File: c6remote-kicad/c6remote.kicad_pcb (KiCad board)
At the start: 2 copper layers, 37 x 130 mm, 47 parts, among them J1 Battery, Q1 MMBT2222A, SW1 SW_Push, SW10 SW_Push, SW11 SW_Push, SW2 SW_Push, SW3 SW_Push, SW4 SW_Push, SW5 SW_Push, SW6 SW_Push, SW7 SW_Push, SW8 SW_Push, SW9 SW_Push, U1 XIAO-ESP32-C6, U2 TSOP4136, U3 PCF8575DBR

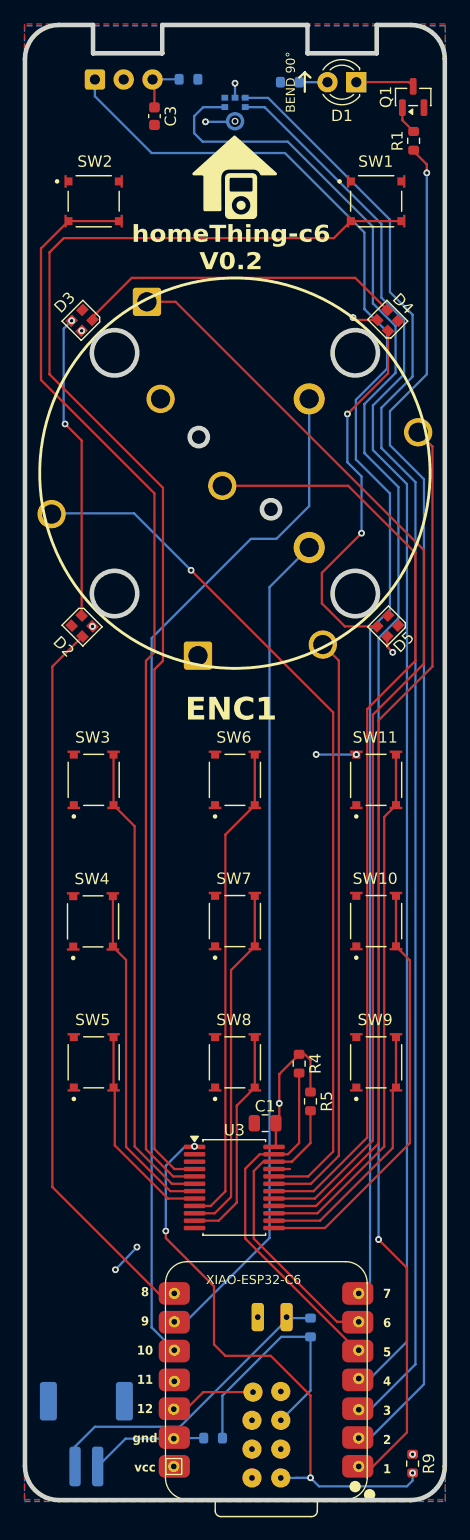
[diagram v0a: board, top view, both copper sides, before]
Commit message: feat(pcb): simplify the top board edge by dropping the two IR cutouts, removing 8 Edge.Cuts segments so the 6.1x2.5mm notches at x 40.837..46.937 and x 59.737..65.837 give way to one straight 31mm line from (37.837455, 28.214) to (68.837455, 28.214) between the corner arcs, neither notch was doing work since U2 topped out at y 31.5 and the D1 dome at y 31.758, both well clear of the old notch floor at y 30.714; the freed strip lets the top row move up, U2 41.0,33.02 to 40.982545,31.262, D1 64.037455,33.258 to 64.0,31.25, R3 and R6 to y 31.25, MK1 53.35,35.99 to 53.35,32.292 and C3 46.25,36.25 to 46.25,34.525, with tracks stretched to follow so segments stay at 289 and vias at 23 while total track length goes 2075.156mm to 2082.025mm, footprints unchanged at 47; zones refilled in the GUI and verified current, a pcbnew ZONE_FILLER pass on a copy reproduces the stored fills exactly with area delta 0 on both the F.Cu GND and +3.3V pours; validated ERC 0, DRC 43 violations 0 errors 0 unconnected parity 13, down from 46 because silk_edge_clearance drops 7 to 4 as three of the four U2 back-silk clips were against the notch walls, all other types unchanged at 24 silk_over_copper, 14 lib_footprint_mismatch and 1 silk_overlap, identical with and without --refill-zones; fab outputs regenerated and export.zip rebuilt from the 11 gerber, job and drill files
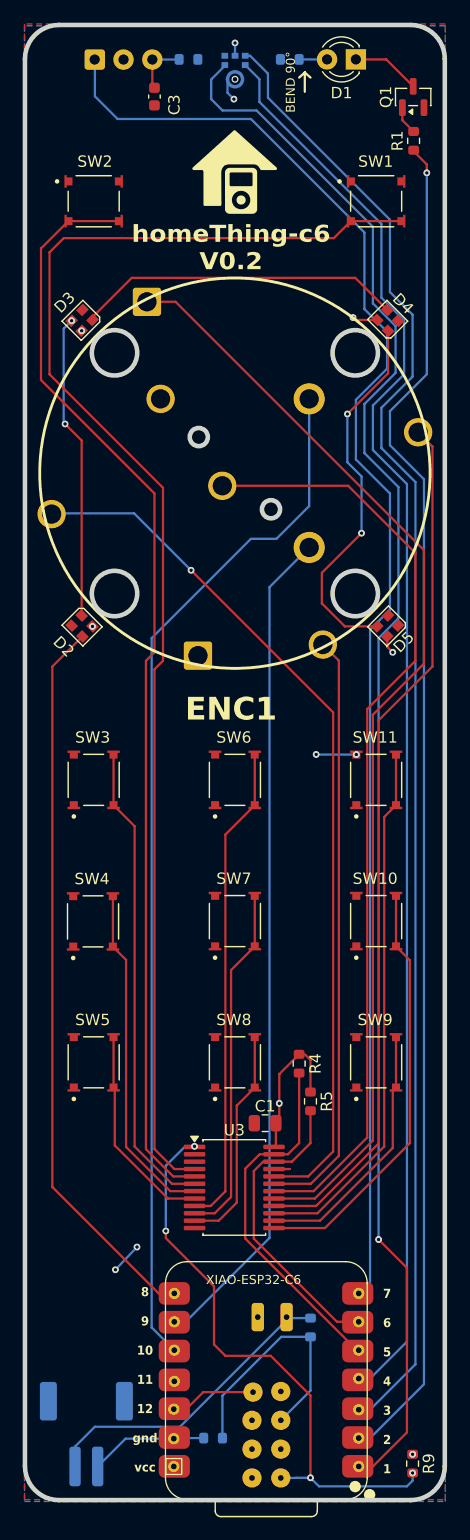
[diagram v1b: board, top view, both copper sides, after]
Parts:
- moved MK1 3.70 mm to (53.4, 32.3)
- moved D1 2.01 mm to (64.0, 31.2)
- moved R3 2.01 mm to (58.2, 31.2)
- moved U2 1.76 mm to (41.0, 31.3)
- moved R6 1.75 mm to (49.2, 31.2)
- moved C3 1.73 mm to (46.2, 34.5)
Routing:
- net sck: track 128.1 -> 130.8 mm
- net ws: track 123.6 -> 126.3 mm
- net IR REC: track 128.1 -> 129.8 mm
- net sd: track 140.4 -> 139.1 mm
- net Net-(D1-K): track 5.17 -> 6.03 mm
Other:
- outline, holes or cut-outs redrawn

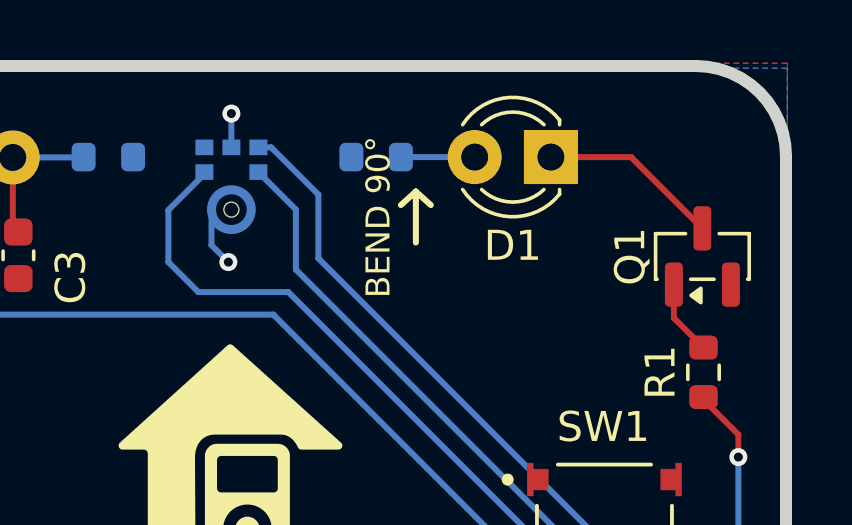
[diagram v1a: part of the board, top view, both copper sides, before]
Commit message: feat(silk): mark the mic port on the front, adding a 2.3mm ring concentric with the MK1 acoustic NPTH at (53.35, 33.002) plus a 1.8mm microphone glyph above it, all five items board graphics on F.SilkS rather than footprint fields so nothing lands in the position file or BOM, ring is a 0.15-wide gr_circle at r 1.15 held under the 1.75mm reach of the neighbouring F.Cu via so its outer edge clears that pad, glyph is a 0.8-wide round-cap gr_line capsule from (53.35, 30.0) to (53.35, 30.3) inside a downward gr_arc bracket (54.2, 30.2) mid (53.35, 31.05) to (52.5, 30.2) with a stem to y 31.05..31.3 and a 1.2mm base at y 31.3, sitting 1.39mm clear of the top board edge; D1 nudged down to y 32.275, R3 across to x 58.425 and the BEND 90 arrow right to x 60.0..61.0 to open the space, tracks following so nets stay intact; zones verified current, a pcbnew ZONE_FILLER pass on a copy reproduces the stored fills exactly with area delta 0 on the GND and +3.3V pours; validated ERC 0, DRC 43 violations 0 errors 0 unconnected parity 13 with the type breakdown unchanged at 24 silk_over_copper, 14 lib_footprint_mismatch, 4 silk_edge_clearance and 1 silk_overlap, so the new silk adds no warnings; fab outputs regenerated and export.zip rebuilt from the 11 gerber, job and drill files
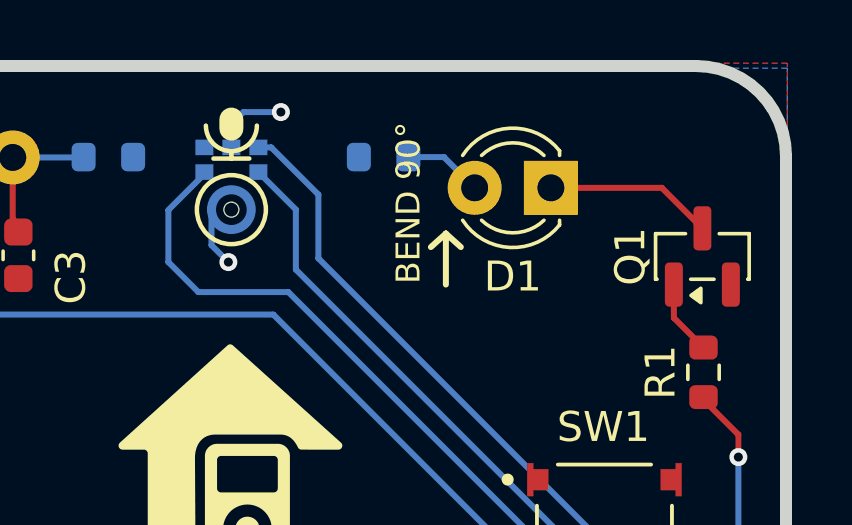
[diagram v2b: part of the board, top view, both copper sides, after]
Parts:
- moved D1 1.02 mm to (64.0, 32.3)
- moved R3 0.25 mm to (58.4, 31.2)
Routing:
- net GND: track 21.2 -> 22.6 mm
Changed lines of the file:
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@@
 	(footprint "LED_THT:LED_D3.0mm_IRBlack"
 		(layer "F.Cu")
-		(at 64 31.25 180)
+		(at 64 32.275 180)
 		(descr "LED, diameter 3.0mm, 2 pins, infrared, black, generated by kicad-footprint-generator")
 		(tags "LED IR")
@@
 		)
 		(point
-			(at 62.73 31.25)
+			(at 62.73 32.275)
 			(size 2)
 			(layer "F.Fab")
@@
 	(footprint "Resistor_SMD:R_0603_1608Metric"
 		(layer "B.Cu")
-		(at 58.175 31.25)
+		(at 58.425 31.25)
 		(descr "Resistor SMD 0603 (1608 Metric), square (rectangular) end terminal, IPC-7351 nominal, (Body size source: IPC-SM-782 page 72, https://www.pcb-3d.com/wordpress/wp-content/uploads/ipc-sm-782a_amendment_1_and_2.pdf)")
 		(tags "resistor")
@@
 	)
 	(gr_line
-		(start 59.5 32.4)
-		(end 59 32.85)
+		(start 52.75 31.3)
+		(end 53.95 31.3)
+		(stroke
+			(width 0.15)
+			(type default)
+		)
+		(layer "F.SilkS")
+	)
+	(gr_line
+		(start 53.35 30)
+		(end 53.35 30.3)
+		(stroke
+			(width 0.8)
+			(type default)
+		)
+		(layer "F.SilkS")
+	)
+	(gr_line
+		(start 53.35 31.05)
+		(end 53.35 31.3)
+		(stroke
+			(width 0.15)
+			(type default)
+		)
+		(layer "F.SilkS")
+	)
+	(gr_circle
+		(center 53.35 33.002)
+		(end 54.5 33.002)
+		(stroke
+			(width 0.15)
+			(type default)
+		)
+		(fill no)
+		(layer "F.SilkS")
+	)
+	(gr_arc
+		(start 54.2 30.2)
+		(mid 53.35 31.05)
+		(end 52.5 30.2)
+		(stroke
+			(width 0.15)
+			(type default)
+		)
+		(layer "F.SilkS")
+	)
+	(gr_line
+		(start 60.5 33.8)
+		(end 60 34.25)
 		(stroke
 			(width 0.2)
@@
 	)
 	(gr_line
-		(start 59.5 32.4)
-		(end 60 32.85)
+		(start 60.5 33.8)
+		(end 61 34.25)
 		(stroke
 			(width 0.2)
@@
 	)
 	(gr_line
-		(start 59.5 34.1)
-		(end 59.5 32.4)
+		(start 60.5 35.5)
+		(end 60.5 33.8)
 		(stroke
 			(width 0.2)
@@
 	)
 	(gr_text "BEND 90°"
-		(at 58.25 33.25 90)
+		(at 59.25 32.775 90)
 		(layer "F.SilkS")
 		(effects
@@
 	)
 	(via
-		(at 53.35 29.8)
+		(at 55 29.75)
 		(size 0.6)
 		(drill 0.3)
@@
 	)
 	(segment
+		(start 53.75 29.75)
+		(end 53.35 30.15)
+		(width 0.2)
+		(layer "B.Cu")
+		(net "GND")
+	)
+	(segment
+		(start 53.35 30.15)
+		(end 53.35 30.928)
+		(width 0.2)
+		(layer "B.Cu")
+		(net "GND")
+	)
+	(segment
 		(start 44.709 135.914)
 		(end 42.809 137.914)
@@
 	)
 	(segment
-		(start 53.35 29.8)
-		(end 53.35 30.928)
+		(start 55 29.75)
+		(end 53.75 29.75)
 		(width 0.2)
 		(layer "B.Cu")
@@
 	)
 	(segment
-		(start 69.05 33.625)
-		(end 66.675 31.25)
+		(start 67.7 32.275)
+		(end 64 32.275)
 		(width 0.2)
 		(layer "F.Cu")
@@
 	)
 	(segment
-		(start 66.675 31.25)
-		(end 64 31.25)
+		(start 69.05 33.625)
+		(end 67.7 32.275)
 		(width 0.2)
 		(layer "F.Cu")
@@
 	)
 	(segment
-		(start 59 31.25)
-		(end 61.46 31.25)
+		(start 60.435 31.25)
+		(end 59.25 31.25)
+		(width 0.2)
+		(layer "B.Cu")
+		(net "Net-(D1-A)")
+	)
+	(segment
+		(start 60.435 31.25)
+		(end 61.46 32.275)
 		(width 0.2)
 		(layer "B.Cu")

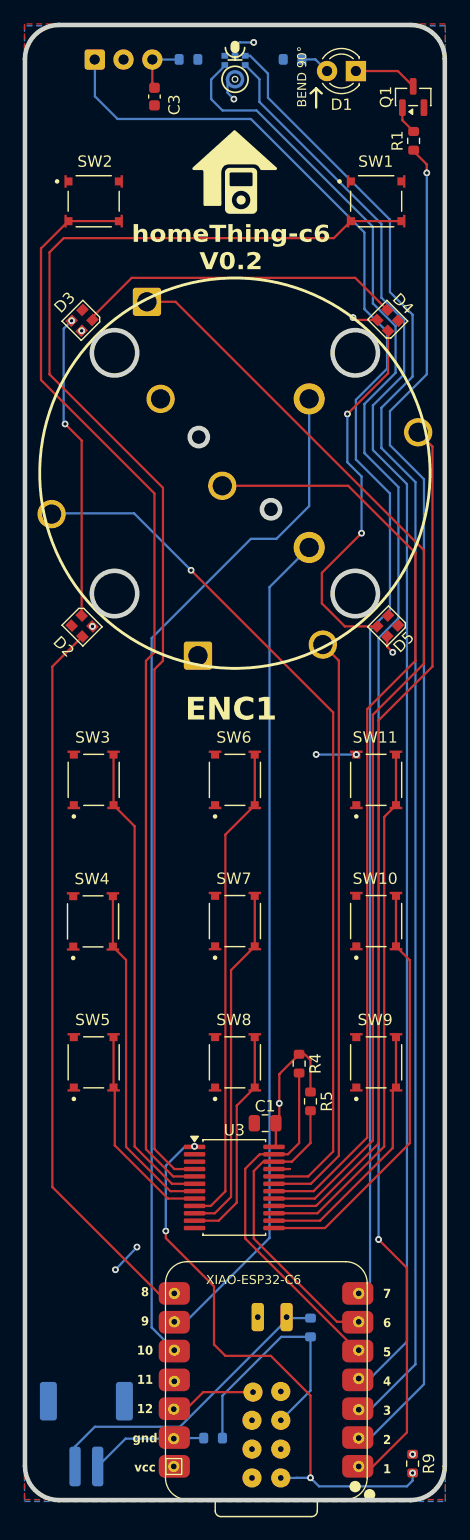
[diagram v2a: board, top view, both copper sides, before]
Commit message: fix(mic): renumber the ICS-43434 symbol pins to the datasheet so MK1 is wired correctly, the embedded INMP441_Microphone_I2S symbol and its project-local inmp441_microphone_i2s.kicad_sym source both carried INMP441 numbering of 1 SCK, 2 WS, 3 L/R, 4 SD, 5 VDD, 6 GND against the ICS-43434 truth in DS-000069 v1.2 Table 8 of 1 WS, 2 LR, 3 GND, 4 SCK, 5 VDD, 6 SD, which put the 3.072MHz bit clock on the mic WS pin, the 48kHz frame clock on LR, left the real SCK pin floating on the undriven sd net and soldered the SD output straight into the GND pour, explaining the bring-up result of 100% zero samples at the correct 192000 B/s byte rate on both channel settings since a mic clocked under 200kHz sits in standby with SD tristated while the ESP samples its own high-Z clock input; the stock Sensor_Audio footprint was already correct with pad N equal to physical pin N, verified against datasheet Fig 3 and Fig 15, so only the symbol changed, pin positions and electrical types untouched so every wire endpoint and net-to-function pairing is preserved; board updated from the schematic with MK1 rotated 180 to 0 in place and the mic cluster rerouted, pads now ws on 1, GND on 2 and 3, sck on 4, +3.3V on 5 and sd on 6, tracks going 289 to 319 segments and 2082.025mm to 2081.778mm with footprints unchanged at 47 and pads at 170, the acoustic NPTH moving to (53.35, 31.582) and the front silk mic ring following to (53.35, 31.575); zones refilled in the GUI and verified current, a pcbnew ZONE_FILLER pass on a copy reproduces the stored fills exactly with area delta 0 on the GND and +3.3V pours; validated ERC 0, DRC 43 violations 0 errors 0 unconnected parity 13 with the type breakdown back at baseline 24 silk_over_copper, 14 lib_footprint_mismatch, 4 silk_edge_clearance and 1 silk_overlap; docs/mic-bringup.md records the root cause and marks the continuity checks superseded because the fault is netlist-level, not assembly
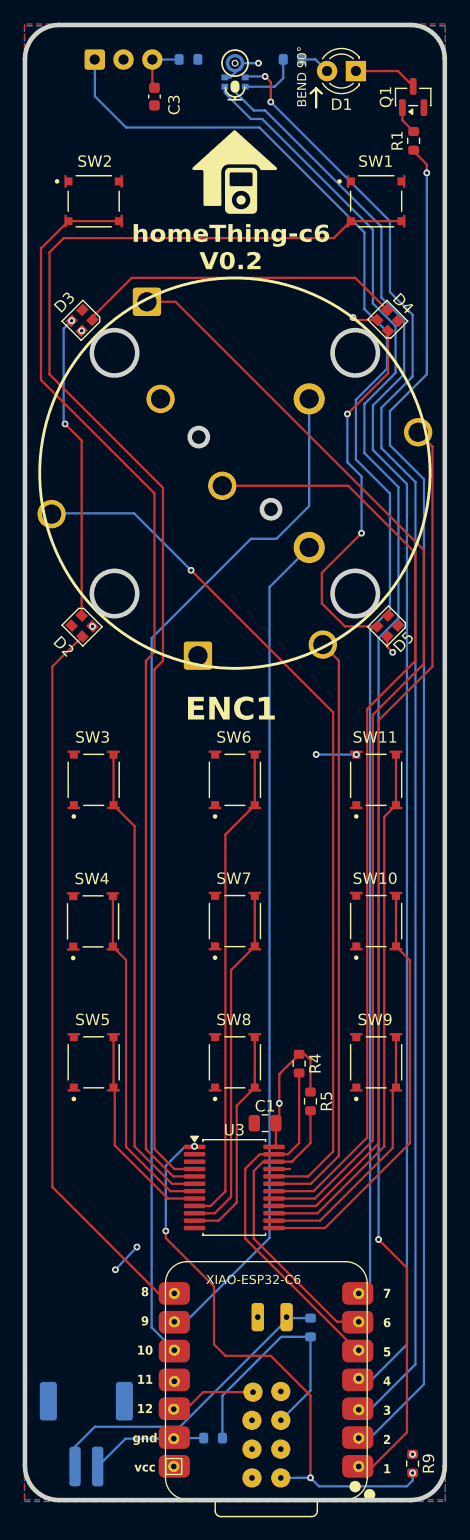
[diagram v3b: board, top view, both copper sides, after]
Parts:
- turned MK1 to 0 degrees
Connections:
- MK1 pad 1: sck -> ws
- MK1 pad 2: ws -> GND
- MK1 pad 4: sd -> sck
- MK1 pad 6: GND -> sd
- TP_SD pad 1: sd -> ws
- TP_WS pad 1: ws -> sd
- U1 pad 1: sd -> ws
- U1 pad 4: ws -> sd
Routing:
- net sd: track 139.1 -> 125.5 mm, vias 1 -> 0
- net ws: track 126.3 -> 135.1 mm, vias 0 -> 1
- net +3.3V: track 24.0 -> 29.3 mm
- net sck: track 130.8 -> 129.8 mm, vias 0 -> 2
- net GND: track 22.6 -> 21.7 mm, vias 6 -> 5

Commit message: feat(led): gate the D2-D5 rail with a high-side P-FET so the four XL-2020RGBC-WS2812B stop burning ~2.4mA quiescent while dark, which was the binding constraint on battery life since a WS2812-class controller die stays powered and listening whenever VDD is present and writing all channels to zero only zeroes PWM duty; Q2 AO3401A (SOT-23, Alpha and Omega, LCSC C15127) puts source on +3.3V, drain on the new led_vdd net feeding all four VDD pads and gate on the new led_en net, with R10 1M pulling the gate to the source so the rail is off by default because GPIO18 boots as a floating input, and Rds(on) 60 milliohm gives 22mV of drop at the 60mA full-white peak; led_en lands on U1 pad 11 (GPIO18/D10), the last unconnected XIAO edge pad, and TP_GPIO18_D10_MOSI now probes it, leaving GPIO6 pad 29 and GPIO7 pad 25 as the only spares; kept high-side so all four LED VSS pads stay zone_connect 2 in the F.Cu GND pour, and the four +3.3V vias that dropped each VDD pad into the B.Cu plane are removed in favour of a led_vdd tree of 39.3mm F.Cu plus 51.9mm B.Cu with 4 vias; C4 1uF 50V X7R 0805 added mid-chain on led_vdd because that plane drop was the whole reason the chain previously needed no decoupling, and it reuses C1's MPN so the BOM groups them into one line; the first routing attempt ran led_vdd diagonally across F.Cu past the wheel and severed the GND pour neck, orphaning D5 VSS in a 77mm2 island as DRC's only unconnected item, so that branch moved to B.Cu and the pour is now 2 islands at 2364.9 and 735.9mm2 with all four LED VSS pads in the main one while the B.Cu +3.3V plane stays a single island at 3348.5mm2; ERC 0, DRC 0 errors and 0 unconnected with the inherited 43 silkscreen and library warnings, parity 13 extra_footprint for the TP_* test points
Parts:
- added C4: 1uF, Capacitor_SMD:C_0805_2012Metric, B.Cu at (46.8, 67.3)
- added Q2: AO3401A, Package_TO_SOT_SMD:SOT-23, F.Cu at (42.0, 84.4)
- added R10: 1M, Resistor_SMD:R_0603_1608Metric, B.Cu at (41.0, 89.6)
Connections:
- D2 pad 4: +3.3V -> led_vdd
- D3 pad 4: +3.3V -> led_vdd
- D4 pad 4: +3.3V -> led_vdd
- D5 pad 4: +3.3V -> led_vdd
- TP_GPIO18_D10_MOSI pad 1: unconnected-(U1-GPIO18_D10_MOSI-Pad11) -> led_en
- U1 pad 11: unconnected-(U1-GPIO18_D10_MOSI-Pad11) -> led_en
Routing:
- net led_vdd: track 0.00 -> 91.2 mm, vias 0 -> 4
- net led_en: track 0.00 -> 67.5 mm, vias 0 -> 1
- net GND: track 21.7 -> 26.9 mm
- net +3.3V: track 29.3 -> 31.9 mm, vias 6 -> 3
